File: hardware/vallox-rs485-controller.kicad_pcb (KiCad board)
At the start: 2 copper layers, 104 x 66 mm, 65 parts, among them J1 + - A B M, J2 TYPE-C-31-M-12, J3 FH12A-12S-0.5SH(55), Q1 AO3400A, SW1 -, SW2 +, SW3 OK, SW4 BACK, U1 ESP32-C3-WROOM-02-N4, U2 TPS54202DDC, U3 ME6211C33M5G-N, U4 THVD1400DR

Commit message: hw(display): J3 entry face at 16.9 mm for real; small cluster moves east
At rotation 270 the FH12's insertion side points toward the glass, so the
previous position put the entry face 8.1 mm out and the 20.7 mm tail ran
past the connector in the render. J3 moves to x 81.1; the RST/DC/backlight
passives move beside it. DRC and parity unchanged.
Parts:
- moved R13 12.2 mm to (89.2, 27.9)
- moved J3 8.80 mm to (81.1, 25.9)
- moved R12 8.65 mm to (86.0, 27.9)
- moved C9 7.57 mm to (86.0, 23.5)
- moved R10 7.57 mm to (86.0, 21.3)
- moved R21 7.57 mm to (86.0, 25.7)
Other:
- board text added: "DS1 glass rests on the board. Tail contacts face the viewer; J3 is a TOP-contact FH12A facing the glass, tail straight, entry face 16.9 mm from the glass edge (x 76.7). Keep the tail path (y 23-29, x 60-77) below 0.8 mm."
- board text removed: "DS1 glass rests on the board. Tail contacts face the viewer; J3 is a TOP-contact FH12A facing the glass, tail straight, entry 16.9 mm from the glass edge. Keep the tail path (y 23-29, x 60-77) below 0.8 mm."
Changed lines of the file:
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@@
 	(footprint "Resistor_SMD:R_0603_1608Metric"
 		(layer "F.Cu")
-		(at 77.5 29.5)
+		(at 86 27.9)
 		(descr "Resistor SMD 0603 (1608 Metric), square (rectangular) end terminal, IPC-7351 nominal, (Body size source: IPC-SM-782 page 72, https://www.pcb-3d.com/wordpress/wp-content/uploads/ipc-sm-782a_amendment_1_and_2.pdf)")
 		(tags "resistor")
 		(property "Reference" "R12"
-			(at 3.036905 0 0)
+			(at 0 1.7036 0)
 			(layer "F.SilkS")
 			(effects
@@
 	(footprint "Resistor_SMD:R_0603_1608Metric"
 		(layer "F.Cu")
-		(at 78.5 26.7)
+		(at 86 25.7)
 		(descr "Resistor SMD 0603 (1608 Metric), square (rectangular) end terminal, IPC-7351 nominal, (Body size source: IPC-SM-782 page 72, https://www.pcb-3d.com/wordpress/wp-content/uploads/ipc-sm-782a_amendment_1_and_2.pdf)")
 		(tags "resistor")
@@
 	(footprint "Resistor_SMD:R_0603_1608Metric"
 		(layer "F.Cu")
-		(at 77.5 31.5)
+		(at 89.2 27.9)
 		(descr "Resistor SMD 0603 (1608 Metric), square (rectangular) end terminal, IPC-7351 nominal, (Body size source: IPC-SM-782 page 72, https://www.pcb-3d.com/wordpress/wp-content/uploads/ipc-sm-782a_amendment_1_and_2.pdf)")
 		(tags "resistor")
 		(property "Reference" "R13"
-			(at 0 1.7036 0)
+			(at 0 -1.7036 0)
 			(layer "F.SilkS")
 			(effects
@@
 	(footprint "Resistor_SMD:R_0603_1608Metric"
 		(layer "F.Cu")
-		(at 78.5 22.3)
+		(at 86 21.3)
 		(descr "Resistor SMD 0603 (1608 Metric), square (rectangular) end terminal, IPC-7351 nominal, (Body size source: IPC-SM-782 page 72, https://www.pcb-3d.com/wordpress/wp-content/uploads/ipc-sm-782a_amendment_1_and_2.pdf)")
 		(tags "resistor")
@@
 		(tags "SOT TO_SOT_SMD")
 		(property "Reference" "Q1"
-			(at -3.125 0 0)
+			(at 0 -2.6736 0)
 			(layer "F.SilkS")
 			(effects
@@
 	(footprint "Connector_FFC-FPC:Hirose_FH12-12S-0.5SH_1x12-1MP_P0.50mm_Horizontal"
 		(layer "F.Cu")
-		(at 72.3 25.92 -90)
+		(at 81.1 25.92 -90)
 		(descr "Hirose FH12, FFC/FPC connector, FH12-12S-0.5SH, 12 Pins per row (https://www.hirose.com/product/en/products/FH12/FH12-24S-0.5SH(55)/)")
 		(tags "connector Hirose FH12 horizontal")
@@
 	(footprint "Capacitor_SMD:C_0603_1608Metric"
 		(layer "F.Cu")
-		(at 78.5 24.5)
+		(at 86 23.5)
 		(descr "Capacitor SMD 0603 (1608 Metric), square (rectangular) end terminal, IPC-7351 nominal, (Body size source: IPC-SM-782 page 76, https://www.pcb-3d.com/wordpress/wp-content/uploads/ipc-sm-782a_amendment_1_and_2.pdf)")
 		(tags "capacitor")
@@
 		(tags "resistor")
 		(property "Reference" "R5"
-			(at -2.655952 0 0)
+			(at 0 -1.7036 0)
 			(layer "F.SilkS")
 			(effects
@@
 		)
 	)
-	(gr_text "DS1 glass rests on the board. Tail contacts face the viewer; J3 is a TOP-contact FH12A facing the glass, tail straight, entry 16.9 mm from the glass edge. Keep the tail path (y 23-29, x 60-77) below 0.8 mm."
+	(gr_text "DS1 glass rests on the board. Tail contacts face the viewer; J3 is a TOP-contact FH12A facing the glass, tail straight, entry face 16.9 mm from the glass edge (x 76.7). Keep the tail path (y 23-29, x 60-77) below 0.8 mm."
 		(at 33.9 46 0)
 		(layer "Cmts.User")

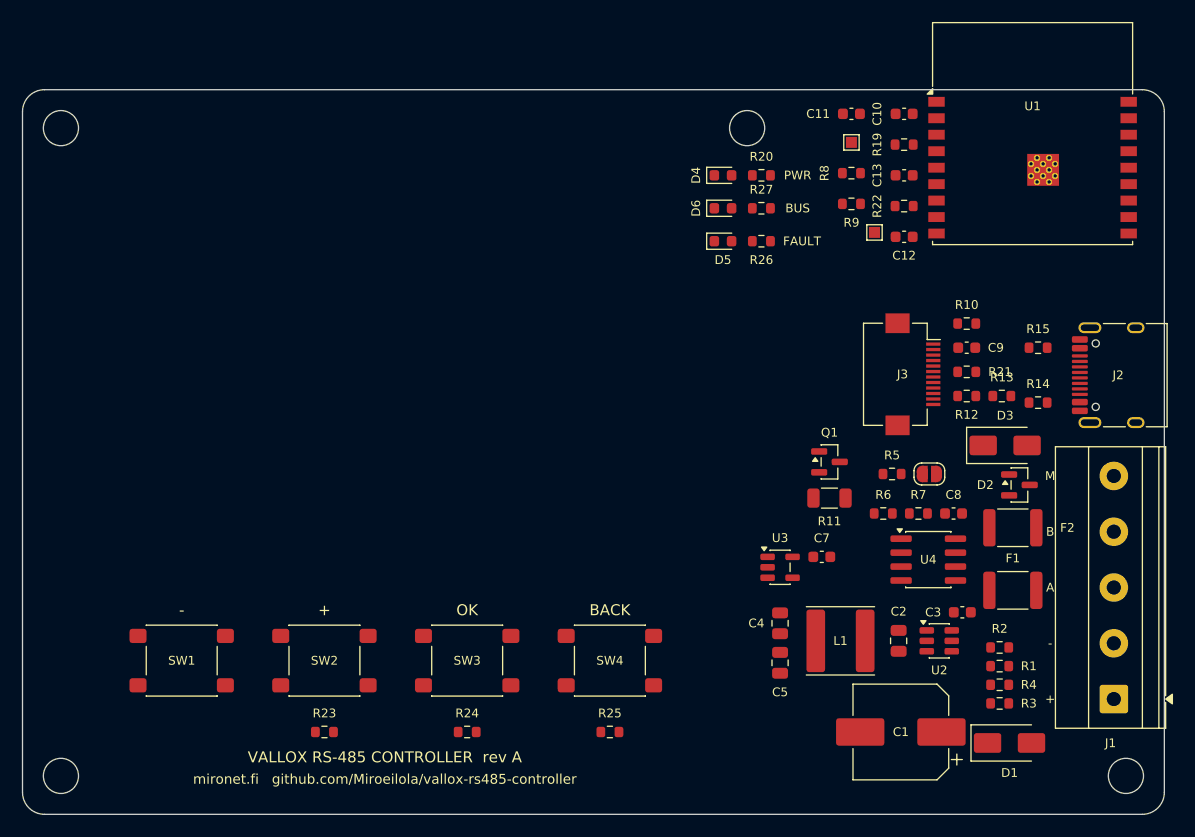
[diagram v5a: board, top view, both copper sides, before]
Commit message: hw(pcb): route the power stage and pour GND on both layers
First routing pass, file-route (pcbnew Python, routes.json is the source of
truth): 21 V input, buck hot loop (SW over the top of C2, BOOT, EN and FB
dividers with R1/R3 turned 180° so the divider taps face each other),
5 V to the LDO, the backlight resistor and the USB OR-diode (one B.Cu
jumper under the 3V3 trunk), 3V3 trunk from the LDO past J3 to the module
and its pull-ups, GND pour F+B with 38 stitch vias. kicad-cli DRC: 0 errors,
8 warnings (baseline set), 138 → 63 unconnected.
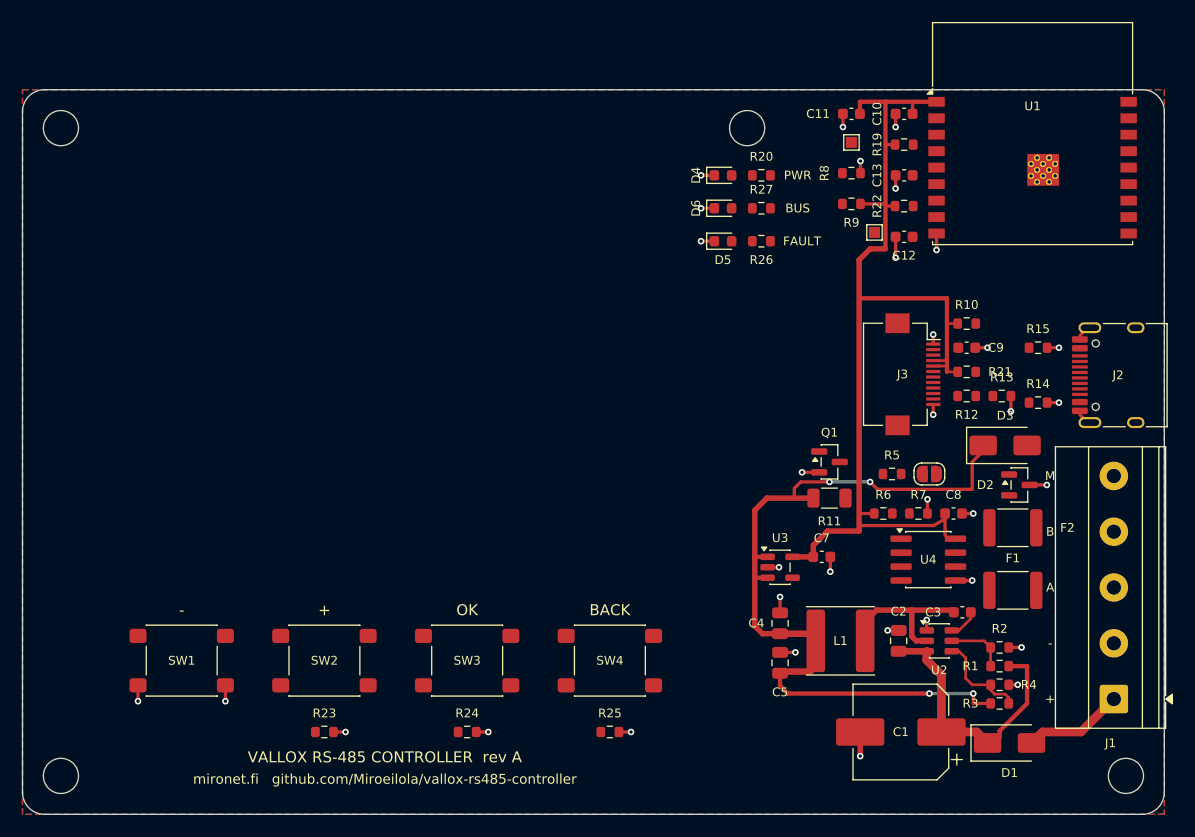
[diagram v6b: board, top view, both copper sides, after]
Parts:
- turned R1 to 180 degrees
- turned R3 to 180 degrees
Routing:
- net +3V3: track 0.00 -> 88.9 mm
- net +5V: track 0.00 -> 67.9 mm, vias 0 -> 4
- net GND: track 0.00 -> 44.5 mm, vias 0 -> 34
- net /VIN_BUCK: track 0.00 -> 24.1 mm
- net /SW: track 0.00 -> 12.1 mm
- net /PANEL_21V: track 0.00 -> 9.16 mm
- net Net-(U2-FB): track 0.00 -> 8.82 mm
- net Net-(U2-EN): track 0.00 -> 5.49 mm
- net Net-(U2-BOOT): track 0.00 -> 2.76 mm
- added copper zone on B.Cu, net GND
- added copper zone on F.Cu, net GND

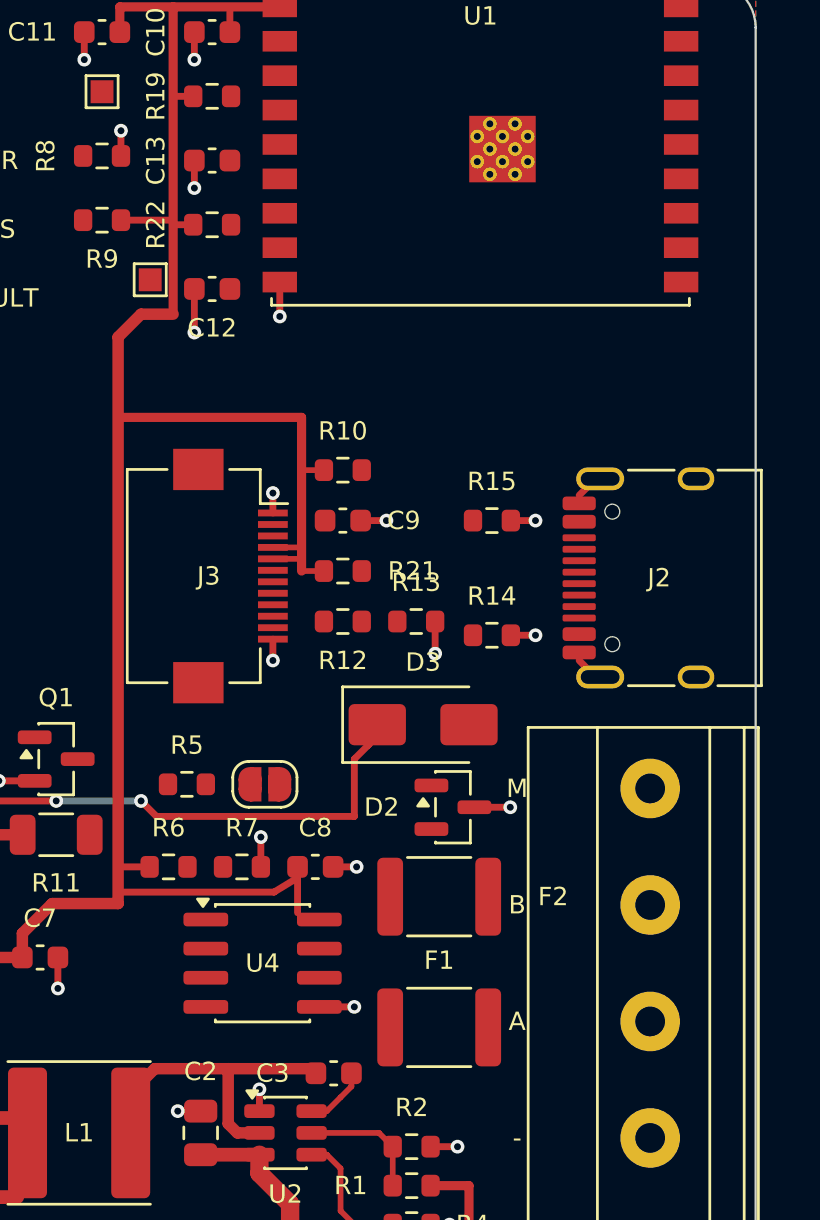
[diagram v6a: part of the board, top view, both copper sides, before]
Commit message: hw(pcb): route the RS-485 front end and USB-C; routes are built by a script
Field terminal to the fuses under each fuse's far pad, TVS and transceiver
A/B with two short B.Cu jumpers (the DNP bias/termination cluster, and
F1's A tail under the J1.4 run), JP1 turned 180° so its B pad faces the
bus, D2.3's GND via moved east. USB-C: D+ pair joined west of the pads,
D- pair east, both to the module's right column on B.Cu clear of the
receptacle's NPTH pegs and its 2.1 mm shield pads; VBUS pad pairs linked
at x 98.9; CC pull-downs. routes.json now comes from
hardware/routing/build_routes.py. DRC 0 errors / 8 baseline warnings,
63 -> 44 unconnected.
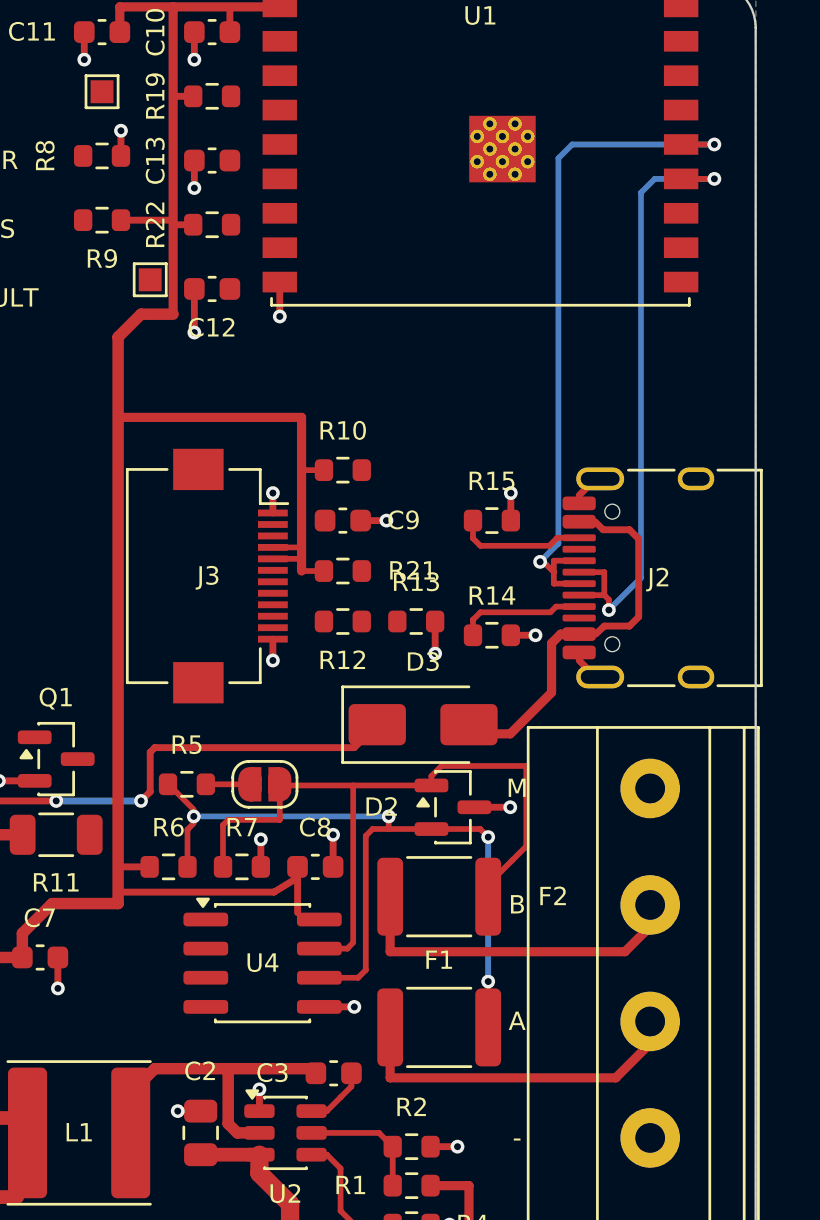
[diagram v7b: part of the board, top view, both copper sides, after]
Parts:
- turned JP1 to 180 degrees
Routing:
- net /RS485_A: track 0.00 -> 32.7 mm, vias 0 -> 4
- net /RS485_B: track 0.00 -> 29.2 mm
- net /USB_D+: track 0.00 -> 28.9 mm, vias 0 -> 2
- net /USB_D-: track 0.00 -> 26.2 mm, vias 0 -> 2
- net /VBUS: track 0.00 -> 14.1 mm
- net Net-(J1-Pin_4): track 0.00 -> 14.0 mm
- net Net-(J1-Pin_3): track 0.00 -> 13.7 mm
- net Net-(J2-CC2): track 0.00 -> 5.08 mm
- net Net-(J2-CC1): track 0.00 -> 5.04 mm
- net +5V: track 67.9 -> 66.3 mm
- net Net-(JP1-B): track 0.00 -> 1.50 mm

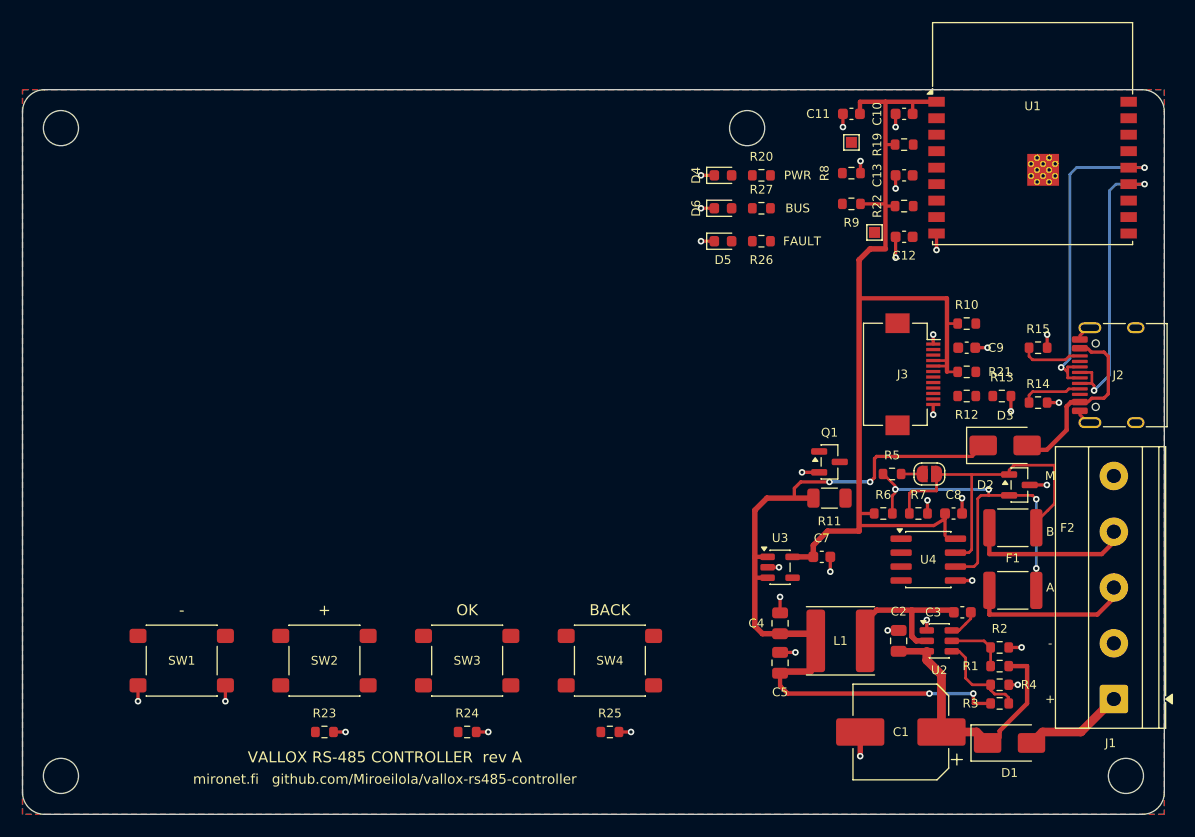
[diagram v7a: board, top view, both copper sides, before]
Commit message: hw(pcb): rev A fully routed — signal nets by Freerouting around the hand-routed power and bus
The 24 remaining low-speed nets (display SPI, UART, buttons, LEDs, EN/BOOT,
backlight) were routed by Freerouting 2.3.0 from a bare DSN with the hand
routes present as fixed obstacles; only those nets' tracks and vias were
merged onto the board, sub-minimum neck-downs widened to 0.2 mm. kicad-cli
DRC with schematic parity: 0 errors, 8 baseline warnings, 0 unconnected.
Method, dead ends and open review items in layout-notes; the decision and
its reasoning in decisions.md.
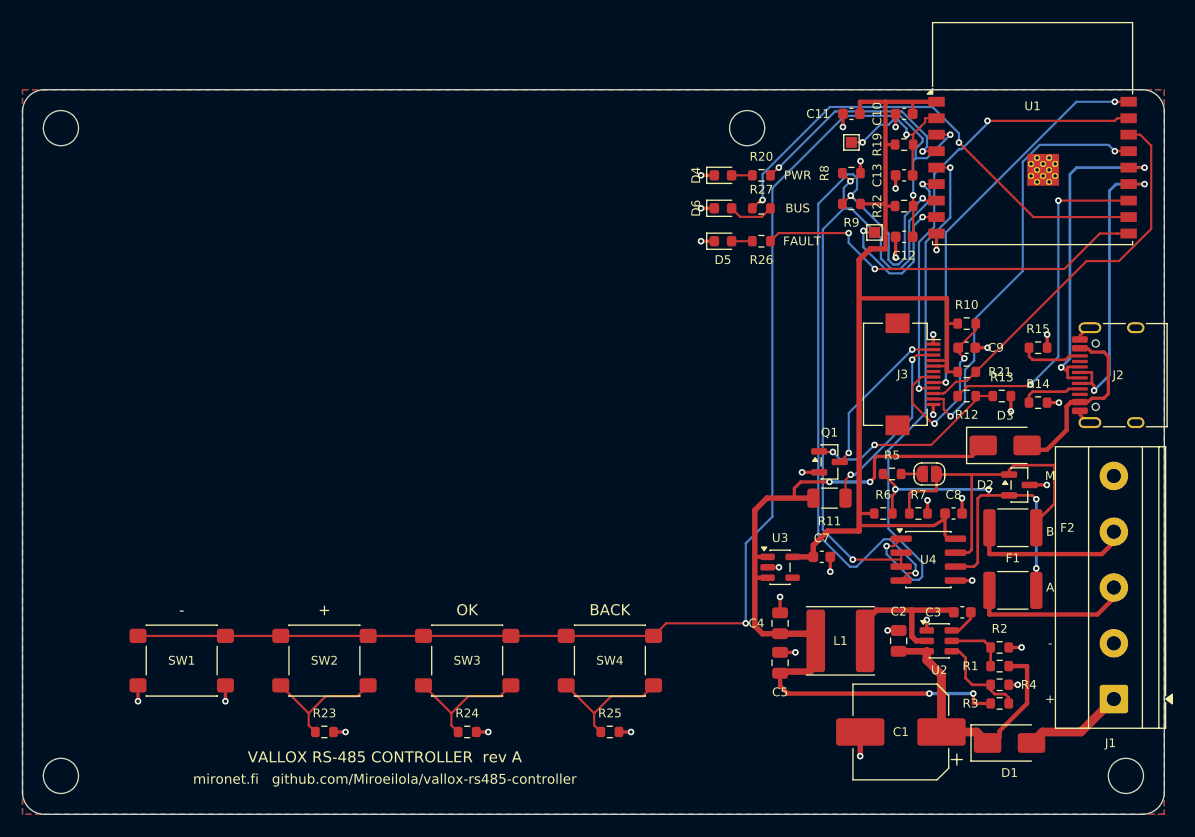
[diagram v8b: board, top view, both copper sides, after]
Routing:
- net /BTN_ADC: track 0.00 -> 128.4 mm, vias 0 -> 3
- net /RS485_TX: track 0.00 -> 68.9 mm, vias 0 -> 3
- net /RS485_DE: track 0.00 -> 62.2 mm, vias 0 -> 3
- net /RS485_RX: track 0.00 -> 48.8 mm, vias 0 -> 2
- net Net-(U1-IO20/RXD): track 0.00 -> 44.1 mm, vias 0 -> 2
- net /TFT_SCK: track 0.00 -> 41.4 mm, vias 0 -> 2
- net /TFT_CS: track 0.00 -> 39.2 mm, vias 0 -> 2
- net /TFT_MOSI: track 0.00 -> 36.4 mm, vias 0 -> 2
- net Net-(U1-IO10): track 0.00 -> 36.1 mm, vias 0 -> 2
- net /TFT_DC: track 0.00 -> 36.1 mm
- net /TFT_BL_PWM: track 0.00 -> 31.3 mm, vias 0 -> 2
- net Net-(U1-IO5): track 0.00 -> 20.4 mm, vias 0 -> 2
- net Net-(Q1-G): track 0.00 -> 18.7 mm, vias 0 -> 2
- net /TFT_RST: track 0.00 -> 17.7 mm, vias 0 -> 2
- net Net-(J3-Pin_3): track 0.00 -> 17.4 mm, vias 0 -> 2
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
